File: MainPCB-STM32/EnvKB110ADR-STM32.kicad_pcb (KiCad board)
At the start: 2 copper layers, 429.5 x 125 mm, 247 parts, among them SW1 Boot Mode, SW2 Reset Switch, U1 XC6206PxxxMR, U2 STM32F411CEUx, Y1 3225_4P 32.768khz

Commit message: Flipped STM32 to other side of board and added a debug header (SWDIO/SWCLK)
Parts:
- added J1: Conn_01x03, Connector_PinHeader_2.54mm:PinHeader_1x03_P2.54mm_Horizontal, B.Cu at (429.0, 55.7)
- C1, C10, C2, C3, C4, C5, C6, C7, C8, C9, R1, R2, R3, R4, R5, R6, R7, SW1, SW2, U1, U2, USB1, Y1: moved to B.Cu
- moved C10 21.0 mm to (429.7, 66.9), turned to 0 degrees
- moved Y1 18.2 mm to (428.1, 64.7), turned to 0 degrees
- moved C3 15.2 mm to (426.9, 67.2), turned to 180 degrees
- moved R7 15.0 mm to (422.7, 59.4)
- moved C9 14.7 mm to (427.5, 62.4), turned to 0 degrees
- moved C8 12.4 mm to (419.4, 56.1), turned to 0 degrees
- moved SW2 11.9 mm to (416.2, 53.4), turned to 180 degrees
- moved R5 11.5 mm to (401.2, 60.7), turned to 180 degrees
- moved R1 9.95 mm to (413.9, 62.6), turned to 0 degrees
- moved C5 8.90 mm to (405.1, 58.3)
- moved C7 8.56 mm to (409.9, 56.6), turned to 270 degrees
- moved R3 7.92 mm to (413.9, 63.6)
- moved R4 7.88 mm to (413.9, 64.7)
- moved U1 7.74 mm to (407.3, 59.0)
- moved R6 6.62 mm to (410.9, 56.6), turned to 270 degrees
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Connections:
- D_104 pad 1: row7 -> col13
- D_105 pad 1: row7 -> col13
- D_106 pad 1: row7 -> col13
- D_107 pad 1: row7 -> col13
- D_108 pad 1: row7 -> col13
- D_109 pad 1: row7 -> col13
- D_110 pad 1: row7 -> col13
- D_111 pad 1: row7 -> col13
- D_112 pad 1: row7 -> col13
- D_113 pad 1: row7 -> col13
- D_114 pad 1: row7 -> col13
- D_115 pad 1: row7 -> col13
- D_116 pad 1: row7 -> col13
- K_110 pad 1: col13 -> row7
- K_23 pad 1: col13 -> row7
- K_61 pad 1: col13 -> row7
- K_82 pad 1: col13 -> row7
- K_98 pad 1: col13 -> row7
- U2 pad 10: row1 -> col20
- U2 pad 11: row3 -> col19
- U2 pad 12: row4 -> col17
- U2 pad 13: row5 -> col16
- U2 pad 14: row6 -> col15
- U2 pad 15: row7 -> col14
- U2 pad 16: col13 -> col12
- U2 pad 17: col0 -> col11
- U2 pad 18: col1 -> col10
- U2 pad 19: col2 -> col9
- U2 pad 20: col3 -> col8
- U2 pad 21: col4 -> col7
- U2 pad 25: col5 -> col6
- U2 pad 26: col6 -> col5
- U2 pad 27: col7 -> col4
- U2 pad 28: col8 -> col3
- U2 pad 29: col9 -> col2
- U2 pad 3: Net-(U2-Pad3) -> col22
- U2 pad 30: col10 -> col1
- U2 pad 31: col11 -> col0
- U2 pad 34: col12 -> row7
- U2 pad 37: col14 -> col13
- U2 pad 38: col15 -> row6
- U2 pad 39: col16 -> row5
- U2 pad 4: Net-(U2-Pad4) -> col21
- U2 pad 40: col17 -> row4
- U2 pad 41: col18 -> row3
- U2 pad 42: col19 -> row1
- U2 pad 43: col20 -> Net-(U2-Pad43)
- U2 pad 45: col21 -> Net-(U2-Pad45)
- U2 pad 46: col22 -> Net-(U2-Pad46)
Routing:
- net col13: track 249.9 -> 522.5 mm, vias 2 -> 3
- net row7: track 498.8 -> 274.2 mm, vias 1 -> 4
- net col20: track 109.2 -> 86.0 mm, vias 1 -> 0
- net col19: track 148.8 -> 126.5 mm, vias 1 -> 0
- net col17: track 194.2 -> 172.4 mm, vias 1 -> 0
- net col16: track 211.2 -> 190.3 mm, vias 1 -> 0
- net PA12: track 22.9 -> 2.77 mm, vias 2 -> 0
- net PA11: track 21.7 -> 1.72 mm, vias 2 -> 0
- net col15: track 227.6 -> 208.4 mm, vias 1 -> 0
- net row3: track 439.6 -> 457.1 mm, vias 1 -> 2
- net col14: track 273.1 -> 255.7 mm, vias 1 -> 0
- net row4: track 445.7 -> 462.8 mm, vias 3 -> 4
- net row5: track 466.6 -> 482.2 mm, vias 1 -> 2
- net col12: track 251.1 -> 236.5 mm, vias 1 -> 0
- net row6: track 483.3 -> 496.9 mm, vias 1 -> 2
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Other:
- board text added: "BOOT"
- board text added: "RESET"
- board text added: "SWCLK"
- board text added: "SWDIO"

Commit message: added mount holes, fixed a couple trace errors, created backplate PCB
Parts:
- added H12: MountingHole, MountingHole:MountingHole_2.2mm_M2_Pad, F.Cu at (326.0, 71.0)
- added H13: MountingHole, MountingHole:MountingHole_2.2mm_M2_Pad, F.Cu at (391.4, 71.0)
- added H14: MountingHole, MountingHole:MountingHole_2.2mm_M2_Pad, F.Cu at (242.7, 71.0)
- added H7: MountingHole, MountingHole:MountingHole_2.2mm_M2_Pad, F.Cu at (156.6, 71.0)
- H1, H10, H2, H3, H4, H5, H6, H8, H9: footprint MountingHole:MountingHole_2.2mm_M2 -> MountingHole:MountingHole_2.2mm_M2_Pad
- moved H1 2.19 mm to (42.9, 73.3)
- moved H9 0.20 mm to (161.4, 117.9)
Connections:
- H1 pad 1: GND -> (no net)
- H10 pad 1: GND -> (no net)
- H2 pad 1: GND -> (no net)
- H3 pad 1: GND -> (no net)
- H4 pad 1: GND -> (no net)
- H5 pad 1: GND -> (no net)
- H6 pad 1: GND -> (no net)
- H8 pad 1: GND -> (no net)
- H9 pad 1: GND -> (no net)
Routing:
- net row4: track 462.8 -> 464.4 mm
- net col22: track 156.9 -> 155.6 mm

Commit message: general adjustments, fixes and tweaks on STM32 version
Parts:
- removed the G*** at (445.4, 63.2)
- added G***: LOGO, logo:lyra, F.Cu at (438.0, 66.0)
- added G***: LOGO, EnvExtras:logo, F.Cu at (400.5, 67.1)
- J1: footprint Connector_PinHeader_2.54mm:PinHeader_1x03_P2.54mm_Horizontal -> Connector_PinSocket_2.54mm:PinSocket_1x03_P2.54mm_Vertical; moved to F.Cu
- K_100, K_101, K_102, K_112, K_113, K_114, K_116, K_12, K_13, K_14, K_15, K_16, K_17, K_18, K_19, K_20, K_21, K_22, K_23, K_24, K_25, K_26, K_27, K_28, K_29, K_30, K_31, K_32, K_33, K_34, K_35, K_36, K_37, K_38, K_39, K_40, K_42, K_43, K_44, K_45, K_46, K_47, K_48, K_50, K_51, K_52, K_53, K_54, K_55, K_56, K_57, K_58, K_59, K_60, K_61, K_63, K_64, K_65, K_66, K_67, K_68, K_71, K_72, K_73, K_74, K_75, K_76, K_77, K_78, K_79, K_80, K_81, K_82, K_83, K_84, K_85, K_87, K_88, K_89, K_90, K_91, K_92, K_93, K_94, K_95, K_96, K_97, K_99: footprint MX_Only:MXOnly-1U-Hotswap -> MX_Only:MXOnly-1U-Hotswap-custom
- K_103, K_115, K_41, K_62, K_69: footprint MX_Only:MXOnly-2U-Hotswap -> MX_Only:MXOnly-1U-Hotswap-custom
- K_104, K_105, K_106, K_108, K_109, K_110, K_111, K_86: footprint MX_Only:MXOnly-1.25U-Hotswap -> MX_Only:MXOnly-1U-Hotswap-custom
- K_107: footprint MX_Only:MXOnly-6.25U-Hotswap-ReversedStabilizers -> MX_Only:MXOnly-1U-Hotswap-custom
- K_49, K_ANSI_3: footprint MX_Only:MXOnly-1.5U-Hotswap -> MX_Only:MXOnly-1U-Hotswap-custom
- K_70: footprint MX_Only:MXOnly-1.75U-Hotswap -> MX_Only:MXOnly-1U-Hotswap-custom
- K_98: footprint MX_Only:MXOnly-2.75U-Hotswap -> MX_Only:MXOnly-1U-Hotswap-custom
- K_ANSI_1, K_ANSI_2: footprint MX_Only:MXOnly-2.25U-Hotswap -> MX_Only:MXOnly-1U-Hotswap-custom
- moved J1 6.36 mm to (423.1, 53.3)
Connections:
- D_104 pad 1: col13 -> row7
- D_105 pad 1: col13 -> row7
- D_106 pad 1: col13 -> row7
- D_107 pad 1: col13 -> row7
- D_108 pad 1: col13 -> row7
- D_109 pad 1: col13 -> row7
- D_110 pad 1: col13 -> row7
- D_111 pad 1: col13 -> row7
- D_112 pad 1: col13 -> row7
- D_113 pad 1: col13 -> row7
- D_114 pad 1: col13 -> row7
- D_115 pad 1: col13 -> row7
- D_116 pad 1: col13 -> row7
- H1 pad 1: (no net) -> GND
- H10 pad 1: (no net) -> GND
- H2 pad 1: (no net) -> GND
- H3 pad 1: (no net) -> GND
- H4 pad 1: (no net) -> GND
- H5 pad 1: (no net) -> GND
- H6 pad 1: (no net) -> GND
- H8 pad 1: (no net) -> GND
- H9 pad 1: (no net) -> GND
- K_110 pad 1: row7 -> col13
- K_23 pad 1: row7 -> col13
- K_61 pad 1: row7 -> col13
- K_82 pad 1: row7 -> col13
- K_98 pad 1: row7 -> col13
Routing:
- net row7: track 274.2 -> 523.5 mm, vias 4 -> 3
- net col13: track 522.5 -> 274.5 mm, vias 3 -> 4
- net col8: track 337.3 -> 355.7 mm
- net col14: track 255.7 -> 267.3 mm
- net col12: track 236.5 -> 240.5 mm
- net col9: track 318.8 -> 322.1 mm
- net Net-(D_62-Pad2): track 29.6 -> 27.9 mm
- net VBUS: track 18.3 -> 19.8 mm
- net resetsw: track 23.1 -> 23.7 mm
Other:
- net class Default: clearance 0.2 -> 0.127
- rule trace_clearance: 0.2 -> 0.127
- board text added: "Designed by"
- board text added: "blackcatplasticworks.com"

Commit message: Corrected inverted traces I think.
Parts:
- removed G***: LOGO, logo:lyra
- removed G***: LOGO, EnvExtras:logo
- removed H12, H13, H14, H7: MountingHole, MountingHole:MountingHole_2.2mm_M2_Pad
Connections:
- U2 pad 1: Net-(U2-Pad1) -> (no net)
- U2 pad 2: Net-(U2-Pad2) -> (no net)
- U2 pad 22: Net-(U2-Pad22) -> (no net)
- U2 pad 43: Net-(U2-Pad43) -> (no net)
- U2 pad 45: Net-(U2-Pad45) -> (no net)
- U2 pad 46: Net-(U2-Pad46) -> (no net)
- USB1 pad 3: Net-(USB1-Pad3) -> (no net)
- USB1 pad 9: Net-(USB1-Pad9) -> (no net)
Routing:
- net col13: track 274.5 -> 275.0 mm, vias 4 -> 6
- net GND: vias 37 -> 38

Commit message: added missing capacitor on vcap
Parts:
- added C11: 2.2uf 0402, Capacitor_SMD:C_0402_1005Metric, B.Cu at (417.6, 71.2)
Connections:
- U2 pad 22: (no net) -> Net-(C11-Pad1)
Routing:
- net Net-(C11-Pad1): track 0.00 -> 2.23 mm

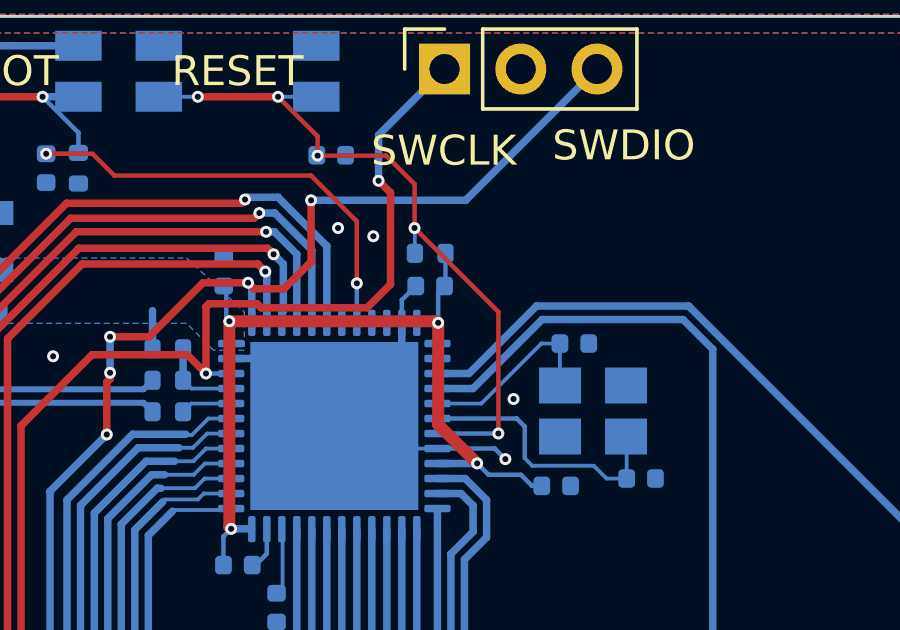
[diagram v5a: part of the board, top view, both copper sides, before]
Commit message: added missing capacitor and power connection
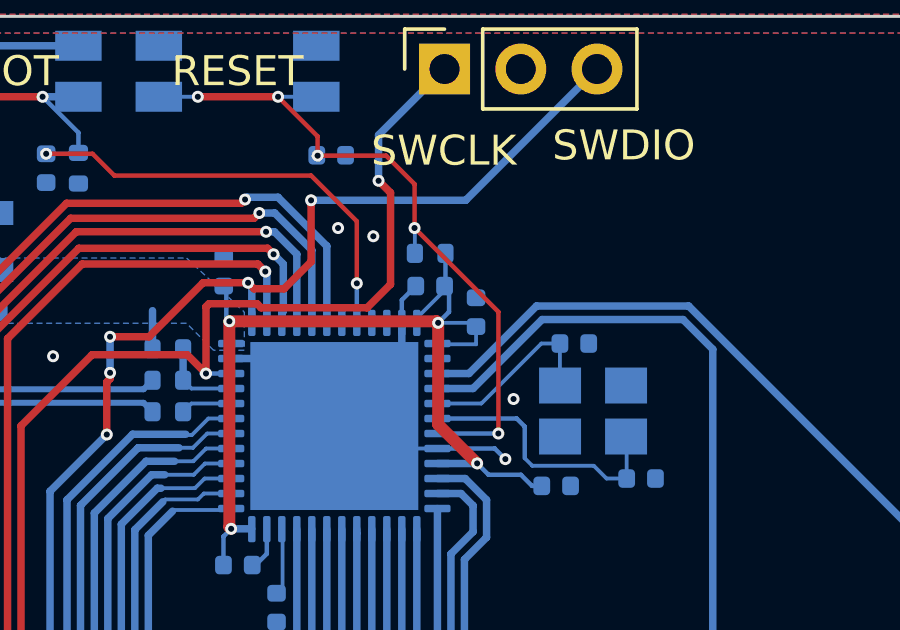
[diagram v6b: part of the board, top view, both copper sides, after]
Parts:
- added C12: 100nf capacitor, Capacitor_SMD:C_0402_1005Metric, B.Cu at (424.2, 61.4)
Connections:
- U2 pad 1: (no net) -> +3V3
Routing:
- net +3V3: track 46.4 -> 50.7 mm
